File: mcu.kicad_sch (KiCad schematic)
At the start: 26 parts, among them J1 ISP Header, J2 USB-C, SW1 SW_Push, U1 ATmega32U4-A, Y1 16MHz

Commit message: end of day. NEARLY DONEgit status!
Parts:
- J2: footprint Connector_USB:USB_C_Receptacle_XKB_U262-16XN-4BVC11 -> Connector_USB:USB_C_Receptacle_HRO_TYPE-C-31-M-12
- R7, R8: footprint Resistor_SMD:R_0603_1608Metric_Pad0.98x0.95mm_HandSolder -> Capacitor_SMD:C_0603_1608Metric_Pad1.08x0.95mm_HandSolder
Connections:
- net COL_0: now also U1.25 (PD4); no longer U1.41 (PF0)
- net COL_1: now also U1.26 (PD6); no longer U1.40 (PF1)
- net COL_10: now also U1.38 (PF5); no longer U1.28 (PB4)
- net COL_11: now also U1.39 (PF4); no longer U1.27 (PD7)
- net COL_12: now also U1.40 (PF1); no longer U1.26 (PD6)
- net COL_13: now also U1.41 (PF0); no longer U1.25 (PD4)
- net COL_2: now also U1.27 (PD7); no longer U1.39 (PF4)
- net COL_3: now also U1.29 (PB5); no longer U1.38 (PF5)
- net COL_4: now also U1.30 (PB6); no longer U1.37 (PF6)
- net COL_5: now also U1.31 (PC6); no longer U1.36 (PF7)
- net COL_6: now also U1.28 (PB4); no longer U1.32 (PC7)
- net COL_7: now also U1.32 (PC7); no longer U1.31 (PC6)
- net COL_8: now also U1.36 (PF7); no longer U1.30 (PB6)
- net COL_9: now also U1.37 (PF6); no longer U1.29 (PB5)

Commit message: needs lots of tidying
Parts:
- renumbered TP8 to TP2, TP9 to TP3
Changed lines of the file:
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@@
   (symbol (lib_id "Connector:TestPoint") (at 170.688 46.101 180) (unit 1)
     (in_bom yes) (on_board yes)
-    (property "Reference" "TP9" (id 0) (at 168.275 51.308 0)
+    (property "Reference" "TP3" (id 0) (at 168.275 51.308 0)
       (effects (font (size 1.27 1.27)) (justify right))
     )
@@
   (symbol (lib_id "Connector:TestPoint") (at 170.688 39.751 0) (unit 1)
     (in_bom yes) (on_board yes)
-    (property "Reference" "TP8" (id 0) (at 168.275 34.671 0)
+    (property "Reference" "TP2" (id 0) (at 168.275 34.671 0)
       (effects (font (size 1.27 1.27)) (justify left))
     )

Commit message: viaing
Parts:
- J2: footprint Connector_USB:USB_C_Receptacle_HRO_TYPE-C-31-M-12 -> Custom:USB_C_Receptacle_HRO_TYPE-C-31-M-12
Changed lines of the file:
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@@
     (property "Reference" "J2" (id 0) (at 71.247 98.2812 0))
     (property "Value" "USB-C" (id 1) (at 71.247 100.8181 0))
-    (property "Footprint" "Connector_USB:USB_C_Receptacle_HRO_TYPE-C-31-M-12" (id 2) (at 75.057 119.761 0)
+    (property "Footprint" "Custom:USB_C_Receptacle_HRO_TYPE-C-31-M-12" (id 2) (at 75.057 119.761 0)
       (effects (font (size 1.27 1.27)) hide)
     )

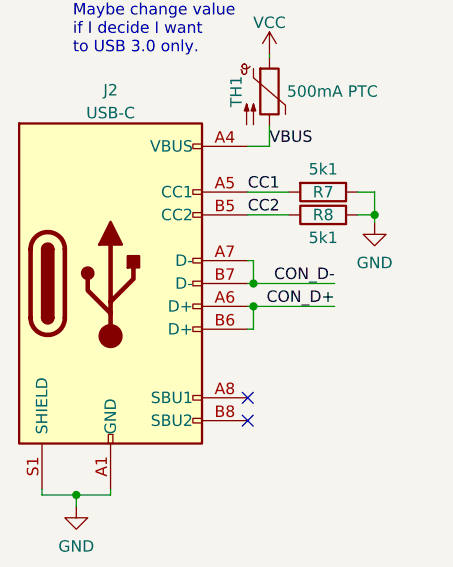
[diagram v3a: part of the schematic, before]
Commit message: updated library references to local
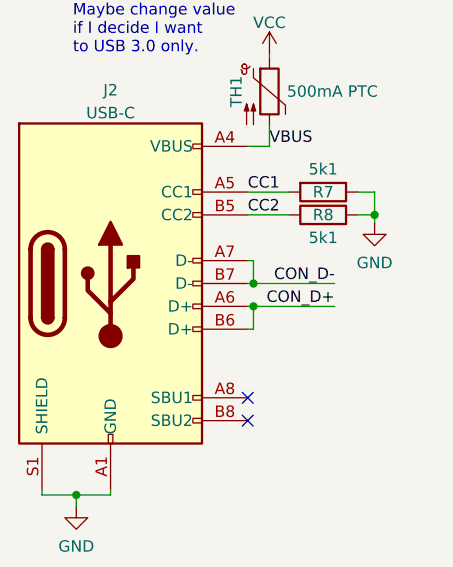
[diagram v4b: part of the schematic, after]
